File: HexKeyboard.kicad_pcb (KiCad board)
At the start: 2 copper layers, 76 parts, among them J1 Micro_SD_Card, J2 Conn_01x04, J3 Conn_02x04_Odd_Even, J5 USB_A, SW1 SW_1, SW10 SW_10, SW11 SW_11, SW12 SW_12, SW13 SW_13, SW14 SW_14, SW15 SW_15, SW16 SW_16, SW17 SW_17, SW18 SW_18, SW19 SW_19, SW2 SW_2, SW20 SW_20, SW21 SW_21, SW22 SW_22, SW23 SW_23, SW24 SW_24, SW25 SW_25, SW3 SW_3, SW4 SW_4, SW5 SW_5, SW6 SW_6, SW7 SW_7, SW8 SW_8, SW9 SW_9, U1 AMS1117-3.3, U2 74LVC125, U3 ATmega32U4-AU, U4 AT24CS64-XHM, U5 MAX7219, Y1 16MHz

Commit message: Finished layout and routing
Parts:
- added H1: MountingHole_Pad, MountingHole:MountingHole_3.2mm_M3_Pad_Via, F.Cu at (36.9, 43.2)
- added H2: MountingHole_Pad, MountingHole:MountingHole_3.2mm_M3_Pad_Via, F.Cu at (159.1, 43.2)
- added H3: MountingHole_Pad, MountingHole:MountingHole_3.2mm_M3_Pad_Via, F.Cu at (36.9, 177.3)
- added H4: MountingHole_Pad, MountingHole:MountingHole_3.2mm_M3_Pad_Via, F.Cu at (159.1, 177.3)
- added H5: MountingHole_Pad, MountingHole:MountingHole_3.2mm_M3_Pad_Via, F.Cu at (152.8, 83.5)
- added H6: MountingHole_Pad, MountingHole:MountingHole_3.2mm_M3_Pad_Via, F.Cu at (152.8, 127.0)
- C3, C7: moved to B.Cu
- moved R4 80.1 mm to (104.5, 54.4)
- moved J2 74.5 mm to (112.0, 49.9), turned to -90 degrees
- moved D26 72.8 mm to (106.9, 54.5)
- moved U1 70.5 mm to (96.0, 59.6)
- moved C2 70.4 mm to (93.9, 65.0)
- moved R6 67.7 mm to (108.3, 40.2)
- moved R7 67.7 mm to (109.5, 42.8)
- moved J5 67.7 mm to (108.7, 42.0)
- moved D27 66.4 mm to (109.5, 54.4)
- moved C4 64.6 mm to (98.7, 65.0), turned to 180 degrees
- moved C3 62.6 mm to (106.0, 62.7), turned to 0 degrees
- moved R5 59.2 mm to (112.1, 54.4)
- moved J3 30.4 mm to (149.8, 59.4)
- moved U4 29.8 mm to (149.0, 99.2)
- moved R1 13.5 mm to (74.6, 55.5)
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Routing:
- net GND: track 6.70 -> 340.7 mm, vias 0 -> 10
- net VCC: track 0.00 -> 220.3 mm, vias 0 -> 5
- net /MISO: track 0.00 -> 115.5 mm, vias 0 -> 1
- net Net-(U3-PB7): track 0.00 -> 100.3 mm, vias 0 -> 1
- net /MOSI: track 0.00 -> 95.0 mm, vias 0 -> 1
- net /SCK: track 0.00 -> 81.5 mm, vias 0 -> 3
- net Net-(U3-PB4): track 0.00 -> 71.6 mm, vias 0 -> 1
- net +3.3V: track 0.00 -> 71.4 mm, vias 0 -> 1
- net /SDA: track 0.00 -> 60.5 mm
- net /SCL: track 0.00 -> 58.6 mm
- net /~{RESET}: track 0.00 -> 30.4 mm, vias 0 -> 1
- net Net-(U3-D+): track 0.00 -> 23.0 mm, vias 0 -> 1
- net Net-(J1-CLK): track 0.00 -> 17.7 mm, vias 0 -> 2
- net Net-(J1-CMD): track 0.00 -> 16.8 mm, vias 0 -> 2
- net Net-(D27-K): track 0.00 -> 16.4 mm, vias 0 -> 1
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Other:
- board outline added: 132.2 x 144.1 mm
- board text added: "Gnd D+ D- VCC"
- board text added: "MOSI NC ~{RST} SCK MISO"
- board text added: "VCC GND GND GND GND"

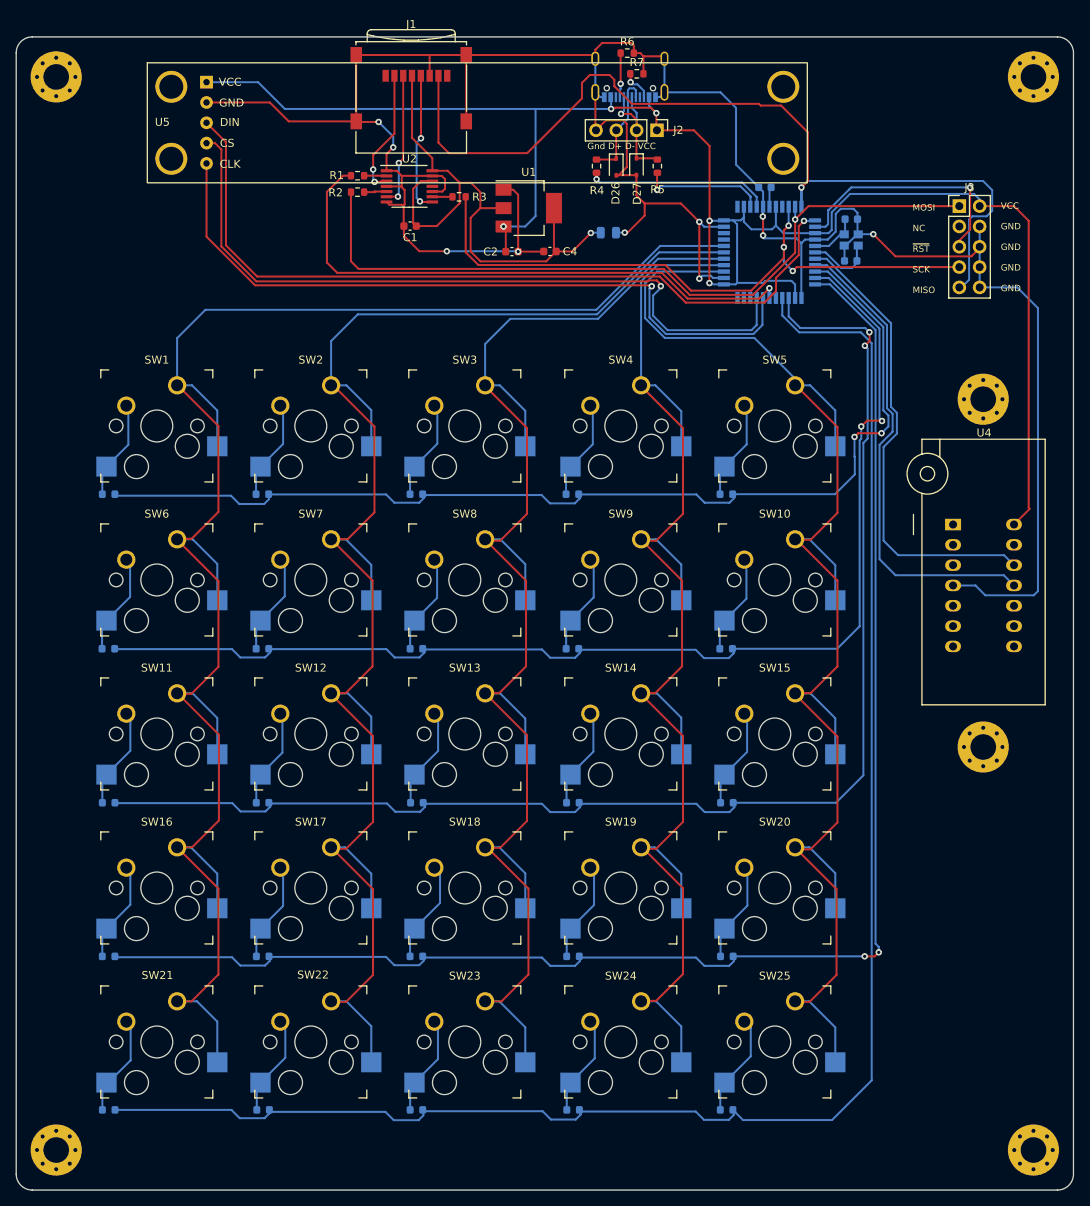
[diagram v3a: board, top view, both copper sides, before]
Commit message: Connected mounting holes to Gnd Added filled zone
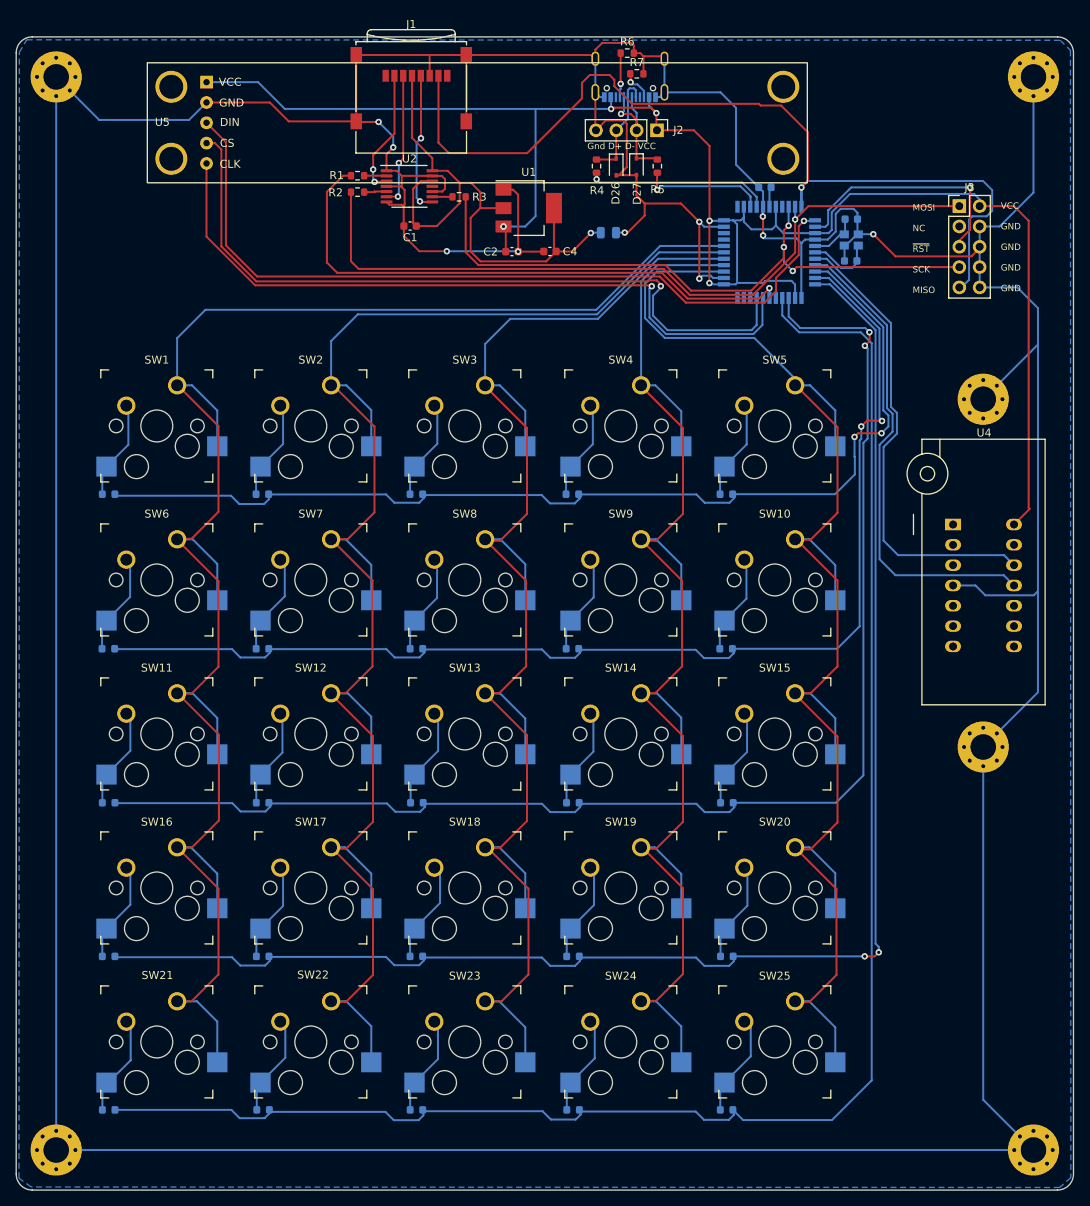
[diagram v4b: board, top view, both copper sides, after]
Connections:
- H1 pad 1: unconnected-(H1-Pad1) -> GND
- H2 pad 1: unconnected-(H2-Pad1) -> GND
- H3 pad 1: unconnected-(H3-Pad1) -> GND
- H4 pad 1: unconnected-(H4-Pad1) -> GND
- H5 pad 1: unconnected-(H5-Pad1) -> GND
- H6 pad 1: unconnected-(H6-Pad1) -> GND
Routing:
- net GND: track 340.7 -> 726.9 mm
- added copper zone on B.Cu, net GND

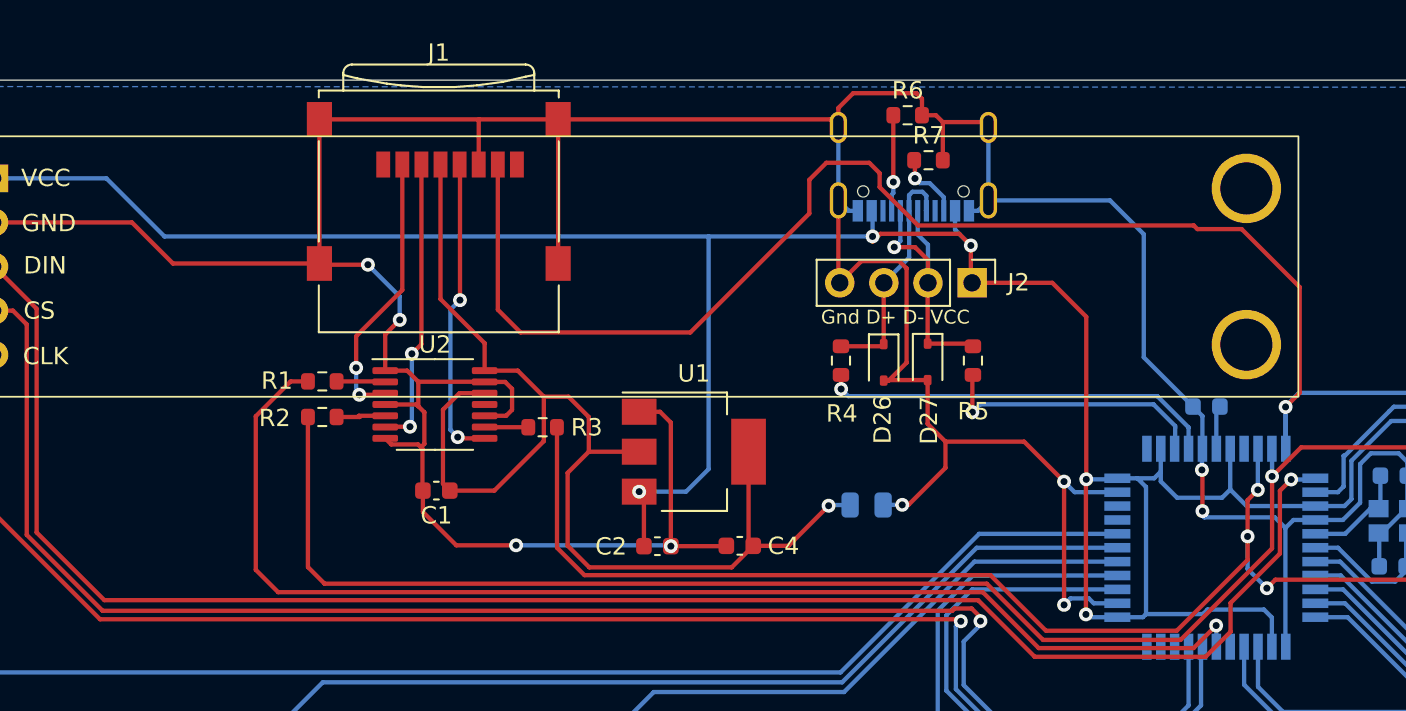
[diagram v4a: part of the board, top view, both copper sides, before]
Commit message: Switched to the correct MicroSD holder
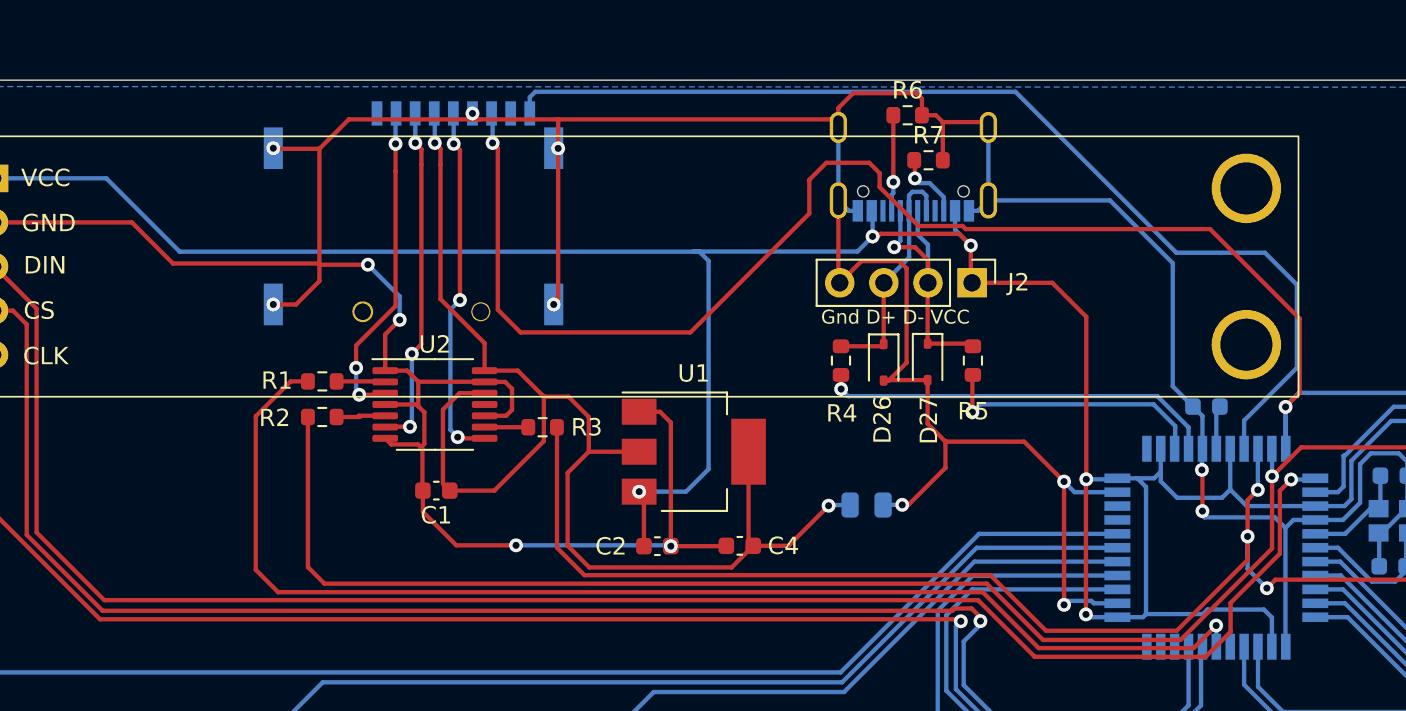
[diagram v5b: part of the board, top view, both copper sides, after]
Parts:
- J1: footprint Connector_Card:microSD_HC_Wuerth_693072010801 -> MicroSD:GCT_MEM2075; moved to B.Cu
- moved J1 7.93 mm to (79.6, 52.4), turned to 180 degrees
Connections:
- net Net-(U3-PB4) renamed /CE
- J1 pad 9: GND -> /CD
- U3 pad 8: unconnected-(U3-PB0-Pad8) -> /CD
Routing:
- net /CD: track 0.00 -> 60.6 mm
- net GND: track 726.9 -> 733.2 mm, vias 10 -> 15
- net +3.3V: track 71.4 -> 74.5 mm, vias 1 -> 2
- net Net-(J1-CLK): track 17.7 -> 20.8 mm, vias 2 -> 3
- net Net-(J1-CMD): track 16.8 -> 19.9 mm, vias 2 -> 3
- net Net-(J1-DAT3/CD): track 16.0 -> 18.8 mm, vias 2 -> 3
- net /MISO: track 115.5 -> 117.5 mm, vias 1 -> 2

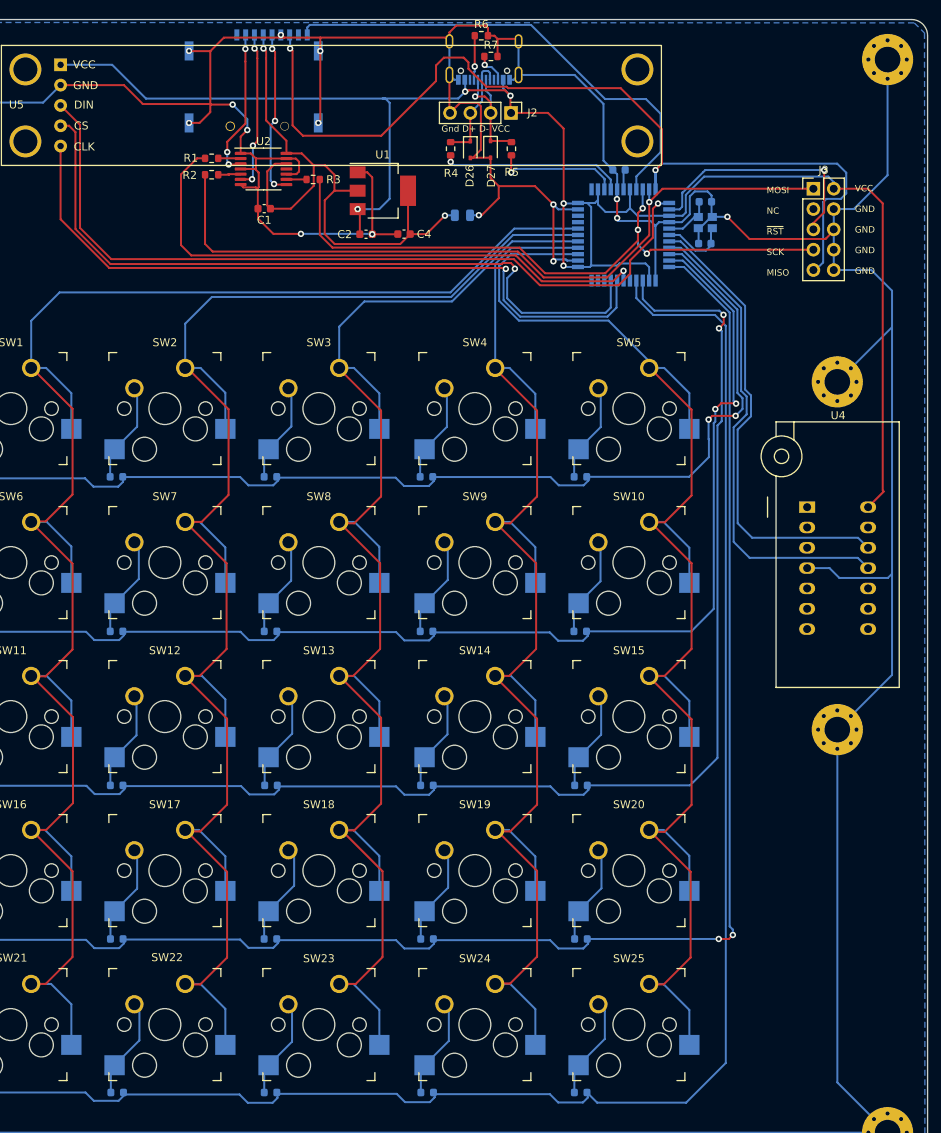
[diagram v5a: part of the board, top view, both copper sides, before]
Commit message: Footprint for SD holder updated. SD holder turned 180 deg USB connector moved out a bit
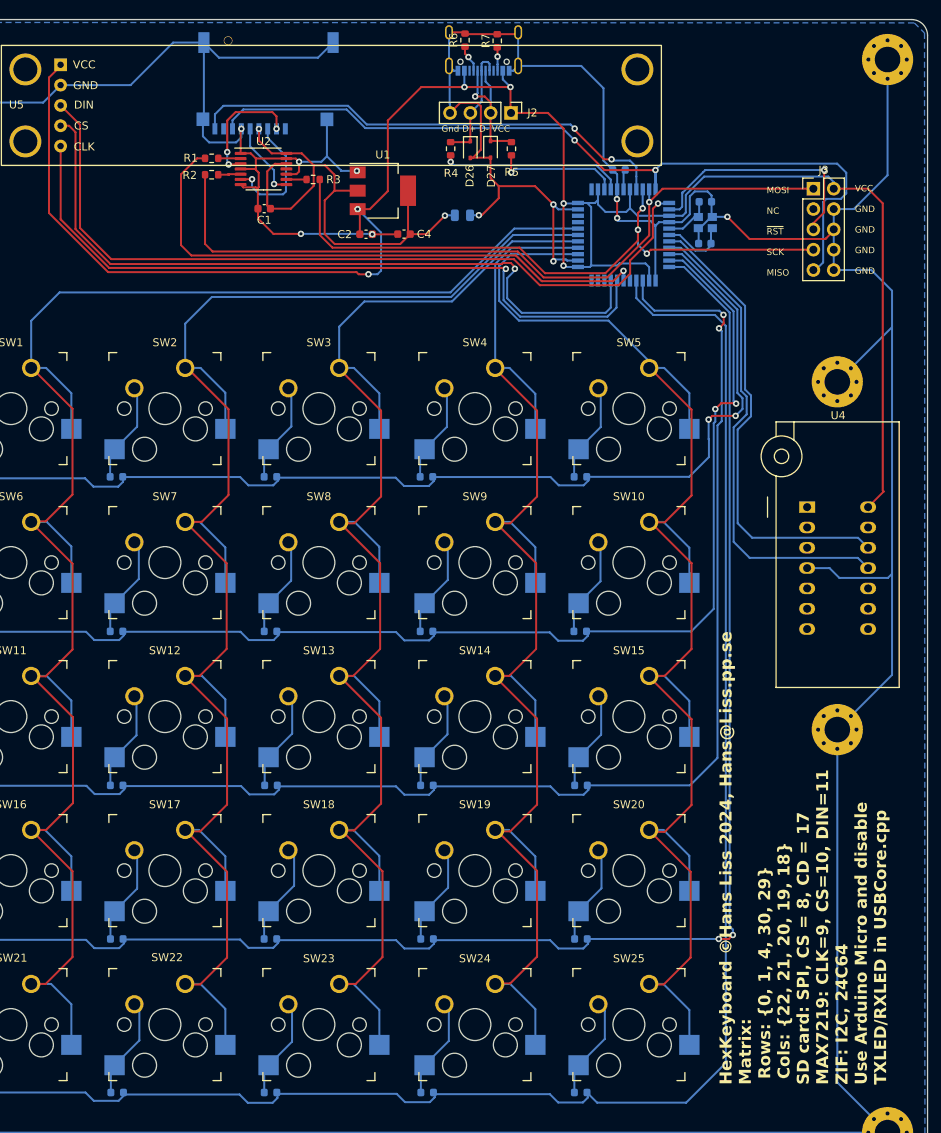
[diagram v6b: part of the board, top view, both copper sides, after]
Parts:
- moved J1 12.6 mm to (81.9, 40.0), turned to 0 degrees
- moved R6 2.12 mm to (106.3, 40.8), turned to 90 degrees
- moved R7 2.11 mm to (110.3, 40.9), turned to 90 degrees
- moved J5 1.13 mm to (108.6, 40.9)
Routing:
- net VCC: track 220.7 -> 249.2 mm, vias 5 -> 6
- net GND: track 733.2 -> 708.8 mm, vias 15 -> 11
- net /MISO: track 117.5 -> 102.2 mm
- net Net-(J1-CLK): track 20.8 -> 9.72 mm, vias 3 -> 1
- net +3.3V: track 74.5 -> 64.1 mm
- net Net-(J1-CMD): track 19.9 -> 15.9 mm, vias 3 -> 1
- net Net-(J1-DAT3/CD): track 18.8 -> 15.5 mm
- net Net-(D27-K): track 16.4 -> 18.6 mm
- net Net-(J5-CC1): track 5.54 -> 3.44 mm
- net Net-(D26-K): track 13.8 -> 14.9 mm
- net Net-(J5-CC2): track 3.96 -> 2.93 mm
- net /CD: track 60.6 -> 61.1 mm, vias 0 -> 2
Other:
- board text added: "HexKeyboard ©Hans Liss 2024, Hans@Liss.pp.se Matrix: Rows: {0, 1, 4, 30, 29} Cols: {22, 21, 20, 19, 18} SD card: SPI, CS = 8, CD = 17 MAX7219: CLK=9, CS=10, DIN=11 ZIF: I2C, 24C64 Use Arduino Micro and disable TXLED/RXLED in USBCore.cpp"
